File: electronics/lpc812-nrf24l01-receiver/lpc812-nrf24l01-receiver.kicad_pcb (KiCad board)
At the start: 2 copper layers, 10 parts, among them K1 CONN_3, K2 CONN_3, K3 CONN_3, K4 CONN_3, P1 CONN_4X2, U1 MCP1703T-3302E/CB, U2 LPC812M101JDH16_TSSOP16

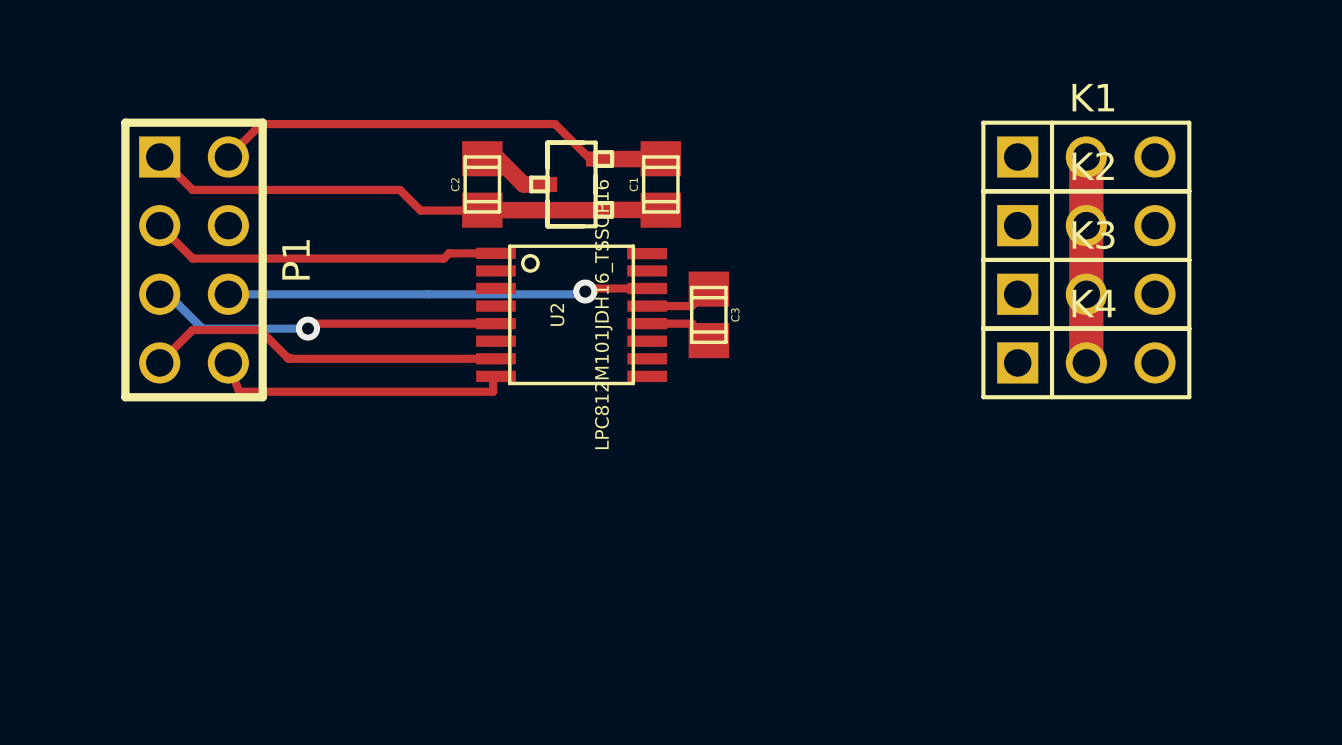
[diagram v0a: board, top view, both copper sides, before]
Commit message: More tweaks to schematics and LPC812 symbol
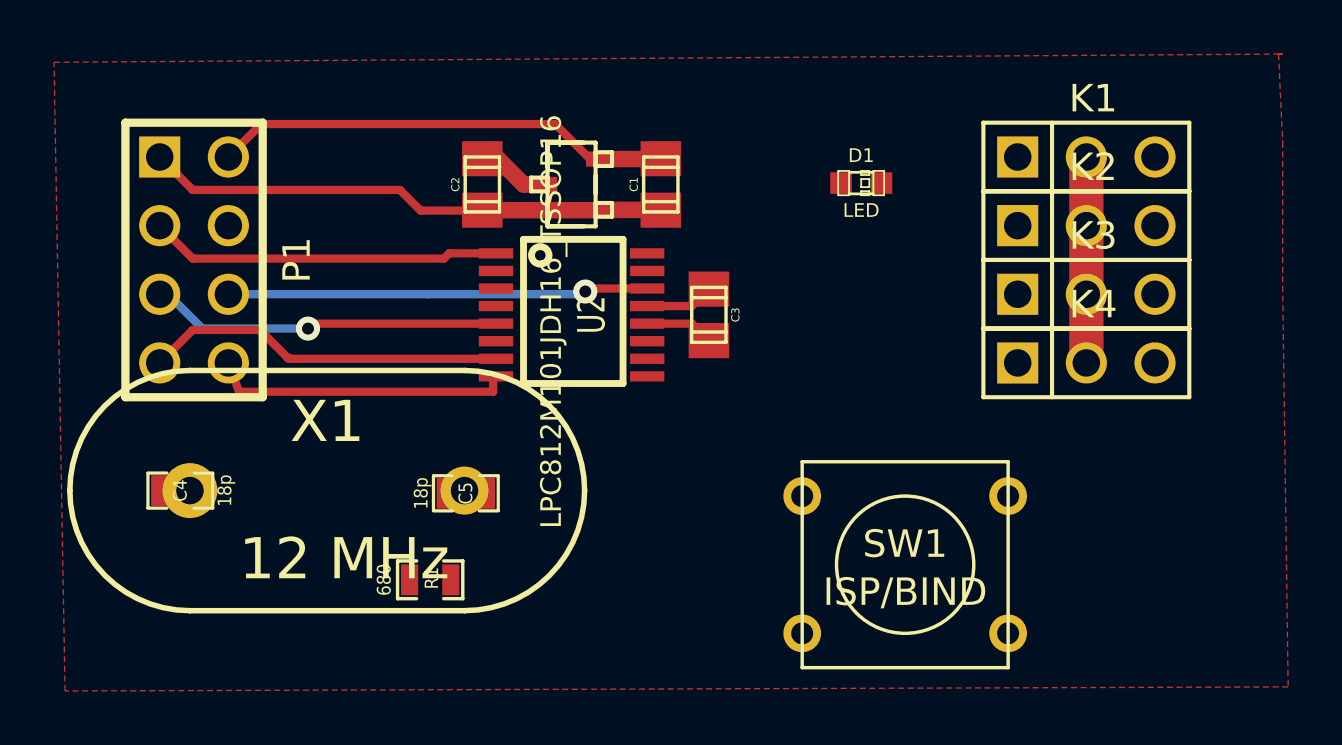
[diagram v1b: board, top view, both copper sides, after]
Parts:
- added C4: 18p, SM0603_Capa, F.Cu at (14.7, 26.3)
- added C5: 18p, SM0603_Capa, F.Cu at (25.3, 26.4)
- added D1: LED, LED-0603, F.Cu at (39.9, 14.9)
- added R1: 680, SM0603_Resistor, F.Cu at (24.0, 29.6)
- added SW1: ISP/BIND, SW_PUSH_SMALL, F.Cu at (41.6, 29.1)
- added X1: 12 MHz, HC-33UV, F.Cu at (20.2, 26.3)
- U2: footprint tssop-16 -> TSSOP16
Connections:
- net Tx renamed CH4/CPPM/Tx
- K2 pad 1: CH3 -> (no net)
- K3 pad 1: TH -> CH2
- K4 pad 1: ST -> CH1
- U2 pad 10: TH -> N-0000018
- U2 pad 11: ST -> N-0000019
- U2 pad 15: CH3 -> CH2
- U2 pad 2: (no net) -> ISP/BIND
- U2 pad 3: (no net) -> LED
- U2 pad 7: MISO -> IRQ
- U2 pad 8: IRQ -> MISO
- U2 pad 9: (no net) -> CH1
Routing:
- net IRQ: track 11.2 -> 22.3 mm
- net MISO: track 13.5 -> 2.34 mm
- added copper zone on F.Cu, net VSS

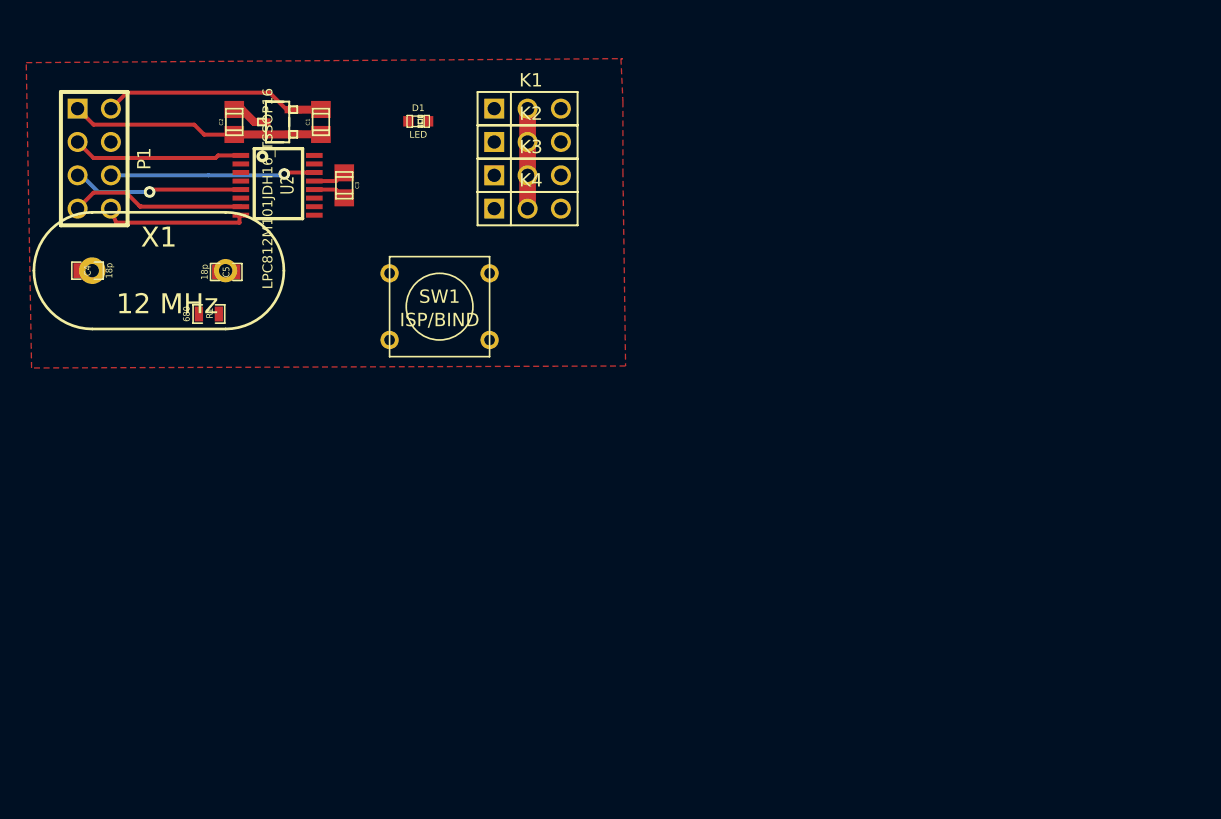
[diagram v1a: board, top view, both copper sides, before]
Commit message: Make ERC pass
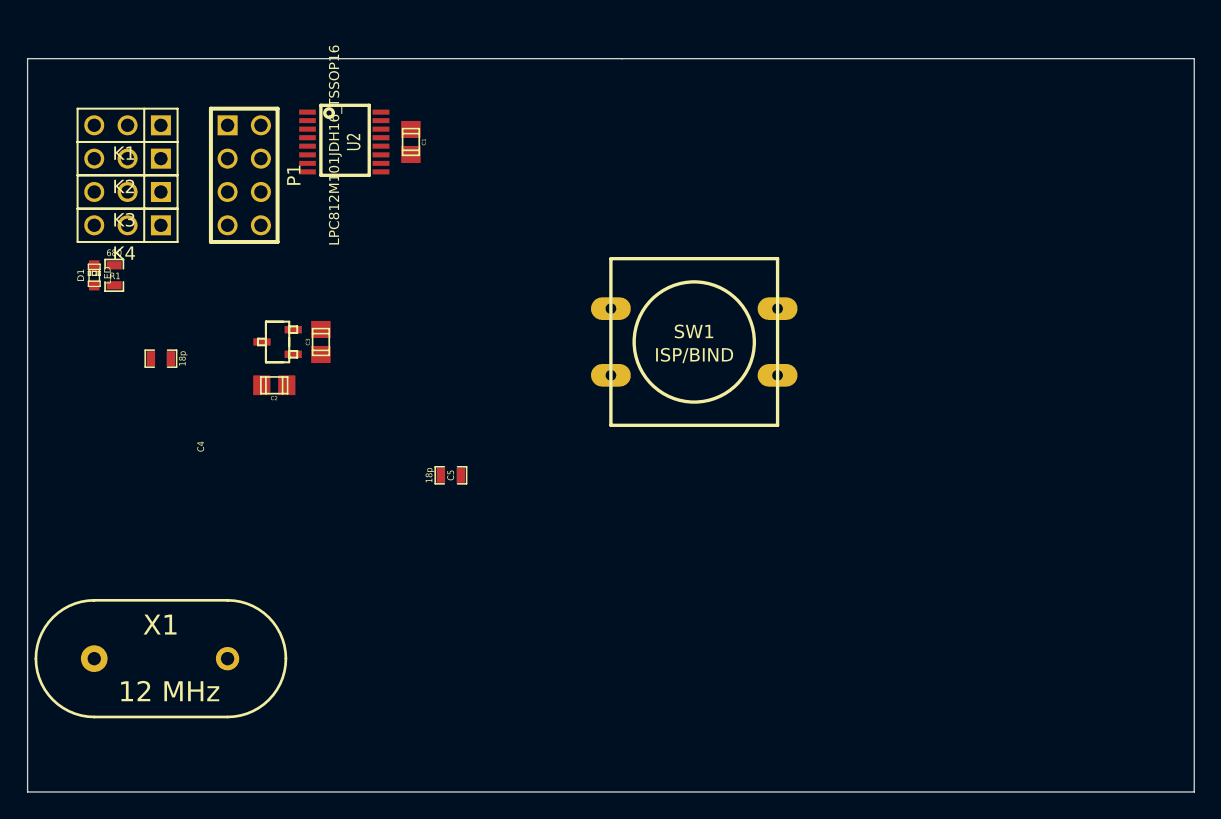
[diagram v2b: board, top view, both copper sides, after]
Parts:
- SW1: footprint SW_PUSH_SMALL -> SW_PUSH-12mm
- moved K1 30.5 mm to (17.8, 15.2), turned to 180 degrees
- moved K2 30.5 mm to (17.8, 17.8), turned to 180 degrees
- moved K3 30.5 mm to (17.8, 20.3), turned to 180 degrees
- moved K4 30.5 mm to (17.8, 22.9), turned to 180 degrees
- moved X1 29.6 mm to (20.3, 55.9)
- moved D1 27.3 mm to (15.2, 26.7), turned to 90 degrees
- moved C5 23.1 mm to (42.4, 41.9)
- moved C2 20.3 mm to (29.0, 35.1), turned to 180 degrees
- moved SW1 19.6 mm to (61.0, 31.8)
- moved U1 16.8 mm to (29.2, 31.8)
- moved C3 12.1 mm to (32.5, 31.8), turned to 90 degrees
- moved P1 11.5 mm to (26.7, 19.1)
- moved C4 8.73 mm to (20.3, 33.0)
- moved R1 7.79 mm to (16.8, 26.7), turned to 270 degrees
- moved C1 7.03 mm to (39.4, 16.5), turned to 270 degrees
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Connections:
- K2 pad 1: (no net) -> CH3/Rx
- U2 pad 16: (no net) -> CH3/Rx
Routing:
- net IRQ: track 22.3 -> 0.00 mm
- net VSS: track 21.9 -> 0.00 mm
- net +3.3V: track 19.6 -> 0.00 mm
- net MOSI: track 15.6 -> 0.00 mm, vias 1 -> 0
- net SCK: track 13.0 -> 0.00 mm, vias 1 -> 0
- net CE: track 13.0 -> 0.00 mm
- net +BATT: track 10.1 -> 0.00 mm
- net MISO: track 2.34 -> 0.00 mm
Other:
- board outline added: 88.9 x 55.9 mm

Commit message: Update board
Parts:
- K1: value CONN_3 -> BAT
- K2: value CONN_3 -> CH3
- K3: value CONN_3 -> TH
- K4: value CONN_3 -> ST
- P1: value CONN_4X2 -> NRF24L01+
- SW1: footprint SW_PUSH-12mm -> SW_PUSH_SMALL
- X1: footprint HC-33UV -> crystal_FA238-TSX3225
- moved SW1 43.2 mm to (17.8, 33.0), turned to 270 degrees
- moved X1 37.5 mm to (34.3, 21.1), turned to 180 degrees
- moved C5 23.9 mm to (31.2, 20.8), turned to 90 degrees
- moved C4 20.9 mm to (37.3, 20.8), turned to 270 degrees
- moved C2 11.0 mm to (22.1, 26.4), turned to 90 degrees
- moved U1 6.55 mm to (25.4, 26.4)
- moved C3 6.55 mm to (28.7, 26.4)
- moved C1 0.36 mm to (39.1, 16.8)
- turned D1 to 270 degrees
- turned R1 to 90 degrees
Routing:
- net ISP/BIND: track 0.00 -> 40.3 mm, vias 0 -> 1
- net LED: track 0.00 -> 28.6 mm
- net +3.3V: track 0.00 -> 22.8 mm
- net CH1: track 0.00 -> 21.5 mm, vias 0 -> 1
- net CH3/Rx: track 0.00 -> 19.8 mm, vias 0 -> 1
- net CH2: track 0.00 -> 19.8 mm, vias 0 -> 1
- net VSS: track 0.00 -> 18.3 mm, vias 0 -> 4
- net +BATT: track 0.00 -> 16.3 mm
- net CE: track 0.00 -> 15.2 mm, vias 0 -> 1
- net CH4/CPPM/Tx: track 0.00 -> 13.2 mm
- net MISO: track 0.00 -> 11.9 mm
- net MOSI: track 0.00 -> 11.7 mm, vias 0 -> 1
- net N-0000018: track 0.00 -> 9.29 mm
- net IRQ: track 0.00 -> 9.24 mm
- net SCK: track 0.00 -> 9.14 mm
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- added copper zone on B.Cu, net VSS
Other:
- board size 88.9 x 55.9 mm -> 29.2 x 26.7 mm

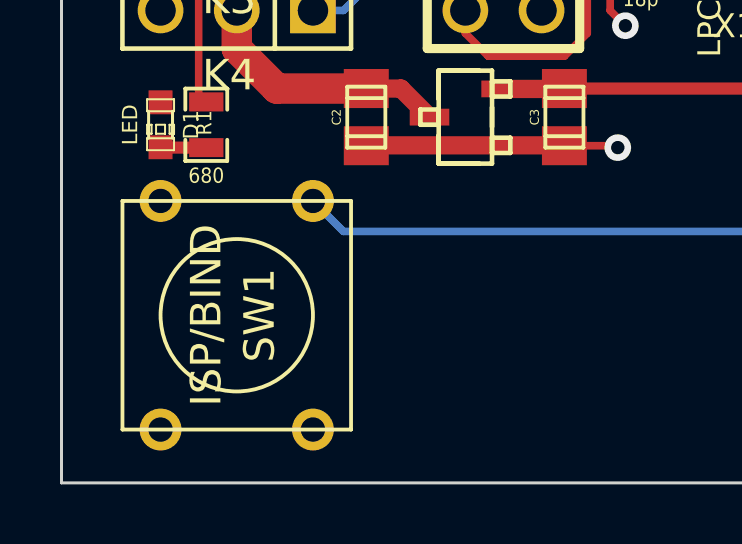
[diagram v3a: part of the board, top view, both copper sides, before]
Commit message: Add switches library for SMD tact switches we have
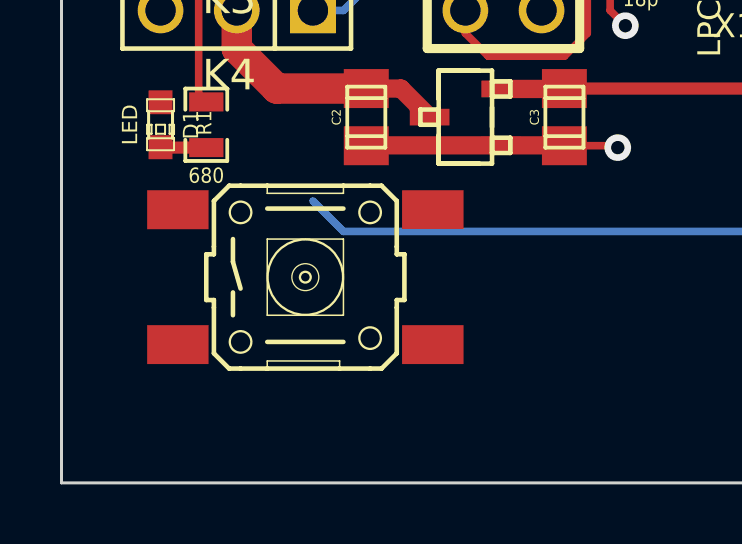
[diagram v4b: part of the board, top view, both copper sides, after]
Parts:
- SW1: footprint SW_PUSH_SMALL -> switches-B3S-10XX
- moved SW1 2.62 mm to (20.1, 31.8), turned to 0 degrees
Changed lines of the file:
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@@
 (kicad_pcb (version 3) (host pcbnew "(2013-jul-07)-stable")
   (general
-    (links 41)
-    (no_connects 4)
+    (links 39)
+    (no_connects 12)
     (area 11.887999 5.887862 55.524401 45.826538)
     (thickness 1.6)
@@
     (19 F.Paste user hide)
     (20 B.SilkS user hide)
-    (21 F.SilkS user hide)
+    (21 F.SilkS user)
     (22 B.Mask user)
     (23 F.Mask user)
@@
     )
   )
-  (module SW_PUSH_SMALL (layer F.Cu)
-    (at 17.78 33.02 270)
-    (fp_text reference SW1 (at 0 -0.762 270) (layer F.SilkS)
-      (effects (font (size 1.016 1.016) (thickness 0.2032)))
-    )
-    (fp_text value ISP/BIND (at 0 1.016 270) (layer F.SilkS)
-      (effects (font (size 1.016 1.016) (thickness 0.2032)))
-    )
-    (fp_circle (center 0 0) (end 0 -2.54) (layer F.SilkS) (width 0.127))
-    (fp_line (start -3.81 -3.81) (end 3.81 -3.81) (layer F.SilkS) (width 0.127))
-    (fp_line (start 3.81 -3.81) (end 3.81 3.81) (layer F.SilkS) (width 0.127))
-    (fp_line (start 3.81 3.81) (end -3.81 3.81) (layer F.SilkS) (width 0.127))
-    (fp_line (start -3.81 -3.81) (end -3.81 3.81) (layer F.SilkS) (width 0.127))
-    (pad 1 thru_hole circle (at 3.81 -2.54 270) (size 1.397 1.397) (drill 0.8128)
-      (layers *.Cu *.Mask F.SilkS)
+  (module switches-B3S-10XX (layer F.Cu)
+    (at 20.066 31.75)
+    (attr smd)
+    (fp_text reference SW1 (at 0.127 -4.318) (layer B.SilkS)
+      (effects (font (size 1.27 1.27) (thickness 0.0889)))
+    )
+    (fp_text value ISP/BIND (at 0.762 4.445) (layer B.SilkS)
+      (effects (font (size 1.27 1.27) (thickness 0.0889)))
+    )
+    (fp_line (start 3.302 0.762) (end 3.048 0.762) (layer F.SilkS) (width 0.1524))
+    (fp_line (start 3.302 0.762) (end 3.302 -0.762) (layer F.SilkS) (width 0.1524))
+    (fp_line (start 3.048 -0.762) (end 3.302 -0.762) (layer F.SilkS) (width 0.1524))
+    (fp_line (start 3.048 -1.016) (end 3.048 -2.54) (layer F.SilkS) (width 0.1524))
+    (fp_line (start -3.302 -0.762) (end -3.048 -0.762) (layer F.SilkS) (width 0.1524))
+    (fp_line (start -3.302 -0.762) (end -3.302 0.762) (layer F.SilkS) (width 0.1524))
+    (fp_line (start -3.048 0.762) (end -3.302 0.762) (layer F.SilkS) (width 0.1524))
+    (fp_line (start 3.048 -2.54) (end 2.54 -3.048) (layer F.SilkS) (width 0.1524))
+    (fp_line (start 2.54 3.048) (end 3.048 2.54) (layer F.SilkS) (width 0.1524))
+    (fp_line (start 3.048 2.54) (end 3.048 1.016) (layer F.SilkS) (width 0.1524))
+    (fp_line (start -2.54 -3.048) (end -3.048 -2.54) (layer F.SilkS) (width 0.1524))
+    (fp_line (start -3.048 -2.54) (end -3.048 -1.016) (layer F.SilkS) (width 0.1524))
+    (fp_line (start -2.54 3.048) (end -3.048 2.54) (layer F.SilkS) (width 0.1524))
+    (fp_line (start -3.048 2.54) (end -3.048 1.016) (layer F.SilkS) (width 0.1524))
+    (fp_line (start -1.27 -1.27) (end -1.27 1.27) (layer F.SilkS) (width 0.0508))
+    (fp_line (start 1.27 1.27) (end -1.27 1.27) (layer F.SilkS) (width 0.0508))
+    (fp_line (start 1.27 1.27) (end 1.27 -1.27) (layer F.SilkS) (width 0.0508))
+    (fp_line (start -1.27 -1.27) (end 1.27 -1.27) (layer F.SilkS) (width 0.0508))
+    (fp_line (start -1.27 -3.048) (end -1.27 -2.794) (layer F.SilkS) (width 0.0508))
+    (fp_line (start 1.27 -2.794) (end -1.27 -2.794) (layer F.SilkS) (width 0.0508))
+    (fp_line (start 1.27 -2.794) (end 1.27 -3.048) (layer F.SilkS) (width 0.0508))
+    (fp_line (start 1.143 2.794) (end -1.27 2.794) (layer F.SilkS) (width 0.0508))
+    (fp_line (start 1.143 2.794) (end 1.143 3.048) (layer F.SilkS) (width 0.0508))
+    (fp_line (start -1.27 2.794) (end -1.27 3.048) (layer F.SilkS) (width 0.0508))
+    (fp_line (start 2.54 3.048) (end 2.159 3.048) (layer F.SilkS) (width 0.1524))
+    (fp_line (start -2.54 3.048) (end -2.159 3.048) (layer F.SilkS) (width 0.1524))
+    (fp_line (start -2.159 3.048) (end -1.27 3.048) (layer F.SilkS) (width 0.1524))
+    (fp_line (start -2.54 -3.048) (end -2.159 -3.048) (layer F.SilkS) (width 0.1524))
+    (fp_line (start 2.54 -3.048) (end 2.159 -3.048) (layer F.SilkS) (width 0.1524))
+    (fp_line (start 2.159 -3.048) (end 1.27 -3.048) (layer F.SilkS) (width 0.1524))
+    (fp_line (start 1.27 -3.048) (end -1.27 -3.048) (layer F.SilkS) (width 0.1524))
+    (fp_line (start -1.27 -3.048) (end -2.159 -3.048) (layer F.SilkS) (width 0.1524))
+    (fp_line (start -1.27 3.048) (end 1.143 3.048) (layer F.SilkS) (width 0.1524))
+    (fp_line (start 1.143 3.048) (end 2.159 3.048) (layer F.SilkS) (width 0.1524))
+    (fp_line (start 3.048 0.762) (end 3.048 1.016) (layer F.SilkS) (width 0.1524))
+    (fp_line (start 3.048 -0.762) (end 3.048 -1.016) (layer F.SilkS) (width 0.1524))
+    (fp_line (start -3.048 0.762) (end -3.048 1.016) (layer F.SilkS) (width 0.1524))
+    (fp_line (start -3.048 -0.762) (end -3.048 -1.016) (layer F.SilkS) (width 0.1524))
+    (fp_line (start -1.27 2.159) (end 1.27 2.159) (layer F.SilkS) (width 0.1524))
+    (fp_line (start 1.27 -2.286) (end -1.27 -2.286) (layer F.SilkS) (width 0.1524))
+    (fp_line (start -2.413 -1.27) (end -2.413 -0.508) (layer F.SilkS) (width 0.1524))
+    (fp_line (start -2.413 0.508) (end -2.413 1.27) (layer F.SilkS) (width 0.1524))
+    (fp_line (start -2.413 -0.508) (end -2.159 0.381) (layer F.SilkS) (width 0.1524))
+    (fp_circle (center 0 0) (end -0.889 0.889) (layer F.SilkS) (width 0.0762))
+    (fp_circle (center -2.159 2.159) (end -2.413 2.413) (layer F.SilkS) (width 0.0762))
+    (fp_circle (center 2.159 2.032) (end 2.413 2.286) (layer F.SilkS) (width 0.0762))
+    (fp_circle (center 2.159 -2.159) (end 2.413 -2.413) (layer F.SilkS) (width 0.0762))
+    (fp_circle (center -2.159 -2.159) (end -2.413 -2.413) (layer F.SilkS) (width 0.0762))
+    (fp_circle (center 0 0) (end -0.3175 0.3175) (layer F.SilkS) (width 0.0254))
+    (fp_circle (center 0 0) (end -0.127 0.127) (layer F.SilkS) (width 0.0762))
+    (fp_text user 1 (at -3.683 -2.286) (layer B.SilkS)
+      (effects (font (size 1.27 1.27) (thickness 0.0889)))
+    )
+    (fp_text user 2 (at 4.191 -2.159) (layer B.SilkS)
+      (effects (font (size 1.27 1.27) (thickness 0.0889)))
+    )
+    (fp_text user 3 (at -3.937 2.159) (layer B.SilkS)
+      (effects (font (size 1.27 1.27) (thickness 0.0889)))
+    )
+    (fp_text user 4 (at 4.191 2.159) (layer B.SilkS)
+      (effects (font (size 1.27 1.27) (thickness 0.0889)))
+    )
+    (pad 1 smd rect (at -4.24942 -2.2479) (size 2.04978 1.29794)
+      (layers F.Cu F.Paste F.Mask)
       (net 10 ISP/BIND)
     )
-    (pad 2 thru_hole circle (at 3.81 2.54 270) (size 1.397 1.397) (drill 0.8128)
-      (layers *.Cu *.Mask F.SilkS)
-      (net 18 VSS)
-    )
-    (pad 1 thru_hole circle (at -3.81 -2.54 270) (size 1.397 1.397) (drill 0.8128)
-      (layers *.Cu *.Mask F.SilkS)
-      (net 10 ISP/BIND)
-    )
-    (pad 2 thru_hole circle (at -3.81 2.54 270) (size 1.397 1.397) (drill 0.8128)
-      (layers *.Cu *.Mask F.SilkS)
-      (net 18 VSS)
-    )
-  )
+    (pad 2 smd rect (at 4.24942 -2.2479) (size 2.04978 1.29794)
+      (layers F.Cu F.Paste F.Mask)
+      (net 18 VSS)
+    )
+    (pad 3 smd rect (at -4.24942 2.2479) (size 2.04978 1.29794)
+      (layers F.Cu F.Paste F.Mask)
+    )
+    (pad 4 smd rect (at 4.24942 2.2479) (size 2.04978 1.29794)
+      (layers F.Cu F.Paste F.Mask)
+    )
+  )
